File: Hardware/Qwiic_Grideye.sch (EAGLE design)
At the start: 26 parts, among them J2 SMD, J3 PTH, J4 SMD, U2 GRIDEYE

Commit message: checklist changes
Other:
- note added: "3.0V-3.6V"
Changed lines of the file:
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@@
 <wire x1="96.52" y1="78.74" x2="96.52" y2="0" width="0.1524" layer="97" style="longdash"/>
 <wire x1="96.52" y1="78.74" x2="248.92" y2="78.74" width="0.1524" layer="97" style="longdash"/>
-<text x="106.68" y="160.02" size="1.778" layer="97">GRIDEye</text>
+<text x="106.68" y="149.86" size="1.778" layer="97">GRIDEye</text>
 <text x="139.7" y="149.86" size="1.778" layer="97">Clear solder jumper JP7
 to disconnect I2C pullups</text>
 <text x="33.02" y="68.58" size="1.778" layer="97">Qwiic/I2C Connections</text>
 <text x="174.498" y="6.858" size="2.54" layer="94">A. England</text>
+<text x="106.68" y="147.32" size="1.27" layer="97">3.0V-3.6V</text>
 </plain>
 <instances>

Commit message: Post double check changes
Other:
- note added: "VCC Range: 3.0V-3.6V"
- note removed: "3.0V-3.6V"
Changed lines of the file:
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@@
 <text x="33.02" y="68.58" size="1.778" layer="97">Qwiic/I2C Connections</text>
 <text x="174.498" y="6.858" size="2.54" layer="94">A. England</text>
-<text x="106.68" y="147.32" size="1.27" layer="97">3.0V-3.6V</text>
+<text x="106.68" y="147.32" size="1.27" layer="97">VCC Range: 3.0V-3.6V</text>
 </plain>
 <instances>

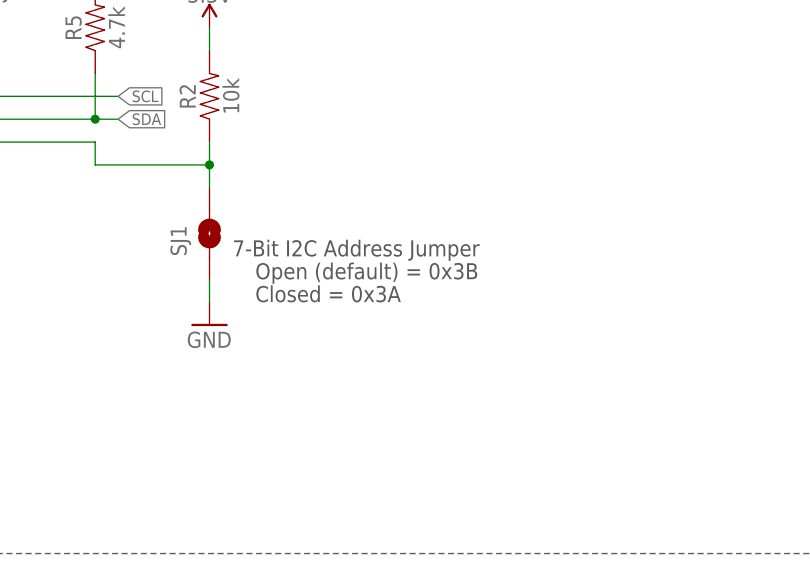
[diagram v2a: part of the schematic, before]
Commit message: updated i2c address
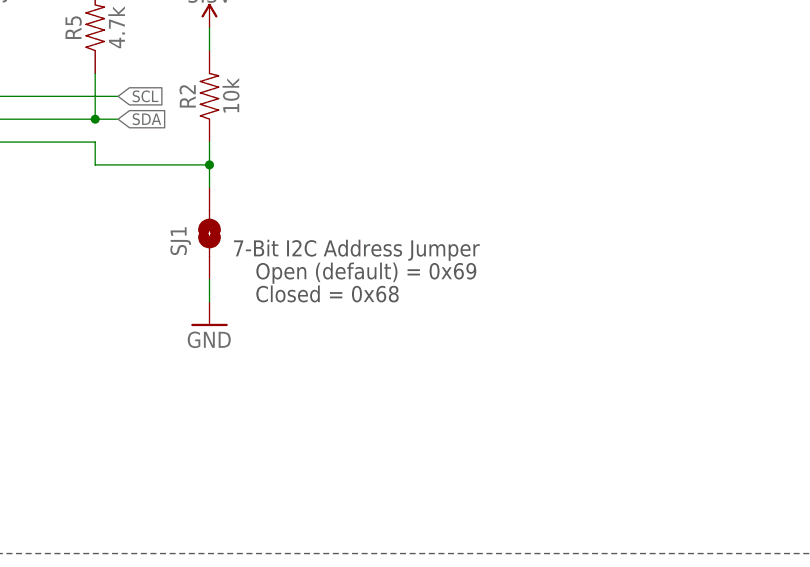
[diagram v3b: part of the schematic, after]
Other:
- note added: "Closed = 0x68"
- note added: "Open (default) = 0x69"
- note removed: "Closed = 0x3A"
- note removed: "Open (default) = 0x3B"
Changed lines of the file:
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@@
 <plain>
 <text x="160.02" y="111.76" size="1.778" layer="97">7-Bit I2C Address Jumper</text>
-<text x="162.56" y="106.68" size="1.778" layer="97">Closed = 0x3A</text>
-<text x="162.56" y="109.22" size="1.778" layer="97">Open (default) = 0x3B</text>
+<text x="162.56" y="106.68" size="1.778" layer="97">Closed = 0x68</text>
+<text x="162.56" y="109.22" size="1.778" layer="97">Open (default) = 0x69</text>
 <text x="170.434" y="11.43" size="2.54" layer="94">N. Seidle</text>
 <text x="237.744" y="7.366" size="2.54" layer="94">v01</text>

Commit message: post checklist changes
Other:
- note added: "v10"
- note removed: "v01"
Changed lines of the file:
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@@
 <text x="162.56" y="109.22" size="1.778" layer="97">Open (default) = 0x69</text>
 <text x="170.434" y="11.43" size="2.54" layer="94">N. Seidle</text>
-<text x="237.744" y="7.366" size="2.54" layer="94">v01</text>
+<text x="237.744" y="7.366" size="2.54" layer="94">v10</text>
 <wire x1="0" y1="78.74" x2="96.52" y2="78.74" width="0.1524" layer="97" style="longdash"/>
 <wire x1="96.52" y1="78.74" x2="96.52" y2="0" width="0.1524" layer="97" style="longdash"/>
